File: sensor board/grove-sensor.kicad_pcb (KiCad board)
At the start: 4 copper layers, 50.8 x 50.8 mm, 45 parts, among them P1 CONN_01X01, P2 CONN_01X06, P3 CONN_01X01, P4 CONN_01X01, P5 CONN_01X01, P6 CONN_01X01, P7 CONN_01X01, P8 CONN_01X01, P9 CONN_01X01, Q1 Q_NPN_BEC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

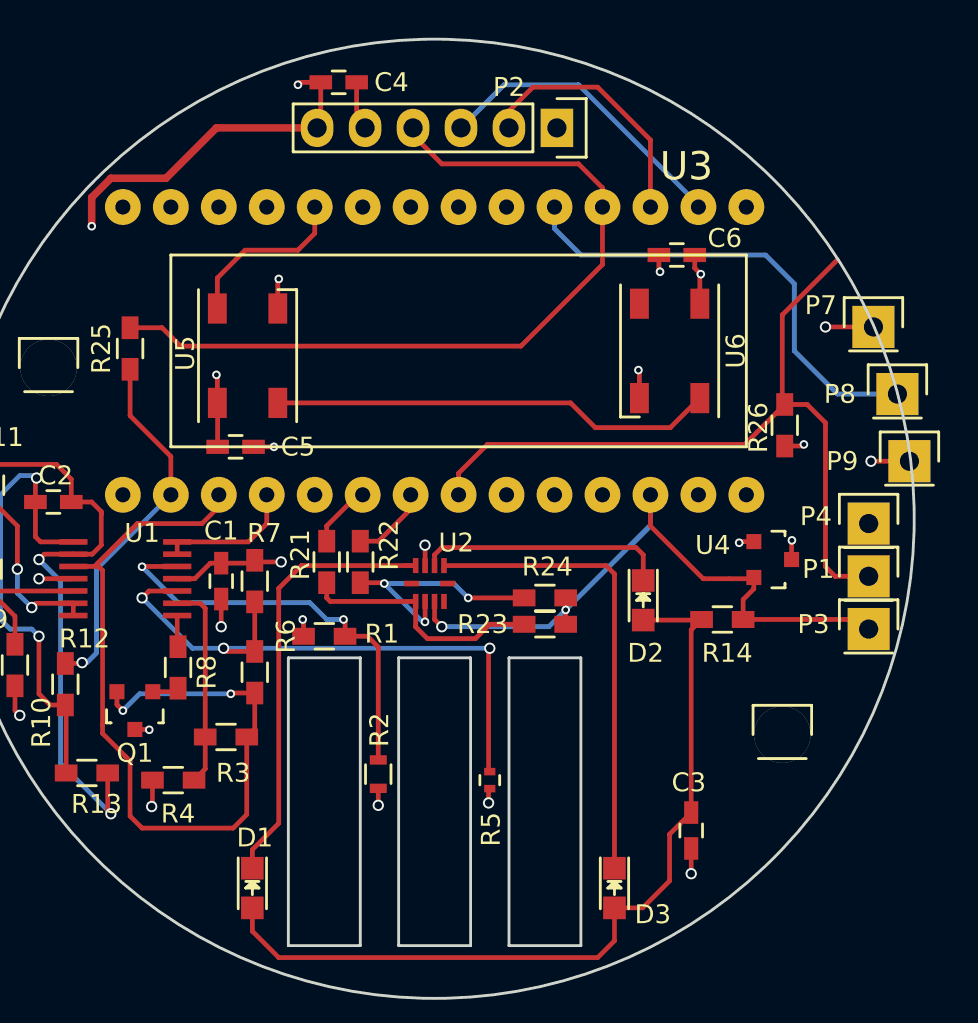
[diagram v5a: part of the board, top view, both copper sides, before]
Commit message: Changes for rev 2 of sensor board
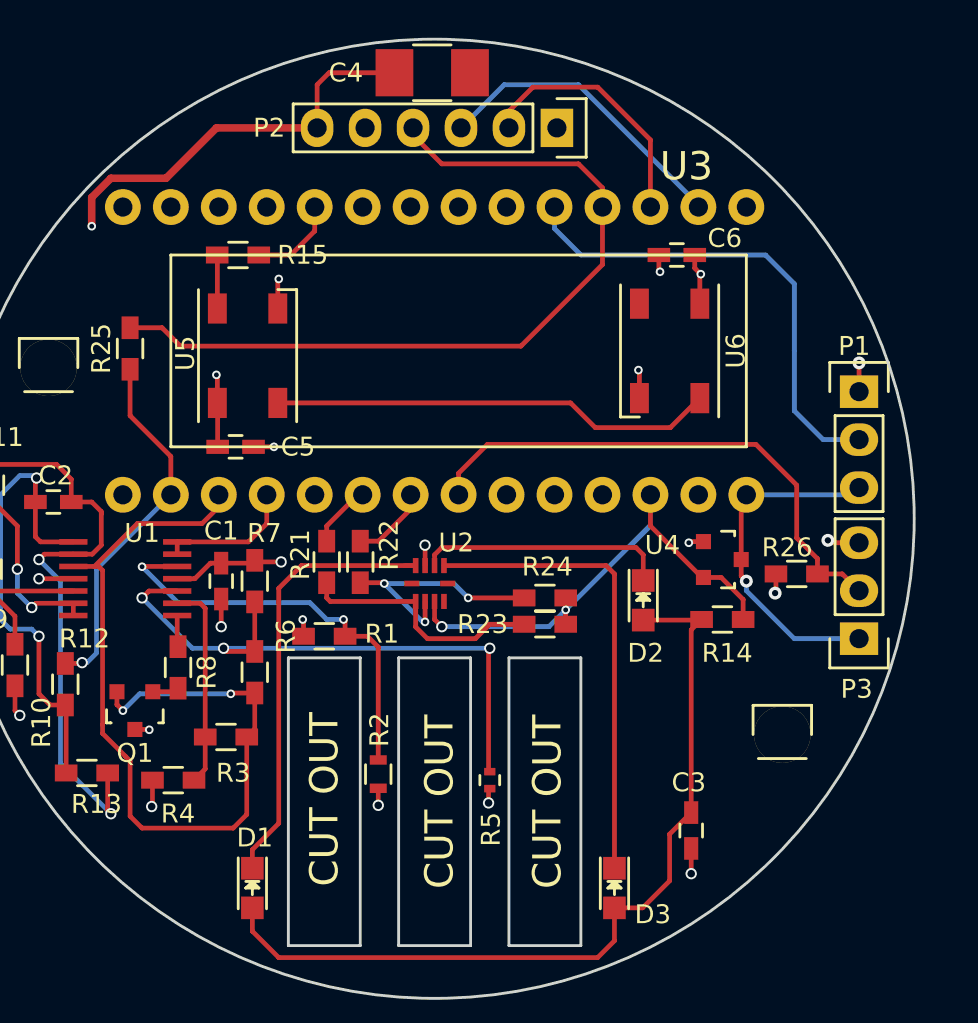
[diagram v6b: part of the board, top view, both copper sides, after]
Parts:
- removed P4, P7, P8, P9: CONN_01X01, Pin_Headers:Pin_Header_Straight_1x01
- added R15: 300, Resistors_SMD:R_0603_HandSoldering, F.Cu at (138.2, 78.7)
- C4: value 10uF -> 100uF; footprint Capacitors_SMD:C_0603_HandSoldering -> Capacitors_SMD:C_1210_HandSoldering
- P1, P3: value CONN_01X01 -> CONN_01X03; footprint Pin_Headers:Pin_Header_Straight_1x01 -> Pin_Headers:Pin_Header_Straight_1x03
- moved P1 9.79 mm to (171.1, 86.0)
- moved R26 7.90 mm to (167.8, 95.6), turned to 0 degrees
- moved C4 4.98 mm to (148.5, 69.1)
- moved U4 2.67 mm to (163.8, 94.9)
- moved P3 0.72 mm to (171.1, 99.1), turned to 180 degrees
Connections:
- P1 pad 1: /PIR_IN -> GND
- P3 pad 1: /3.3V -> +5V
- U3 pad 3: Net-(P8-Pad1) -> Net-(P1-Pad2)
- U3 pad 8: /LED_IN -> Net-(R15-Pad2)
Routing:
- net Net-(P1-Pad2): track 0.00 -> 25.8 mm
- net Net-(P8-Pad1): track 25.0 -> 0.00 mm
- net +5V: track 37.5 -> 55.6 mm, vias 10 -> 8
- net /PIR_IN: track 41.4 -> 28.3 mm
- net /3.3V: track 38.5 -> 30.2 mm
- net /LED_IN: track 9.15 -> 2.84 mm
- net Net-(R15-Pad2): track 0.00 -> 4.76 mm
- net GND: track 22.3 -> 21.3 mm, vias 15 -> 16
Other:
- net class Default: clearance 0.127 -> 0.1524; trace_width 0.4 -> 0.254; via_dia 0.4572 -> 0.6858; via_drill 0.254 -> 0.3302
- net class Power removed
- rule trace_clearance: 0.127 -> 0.1524
- rule trace_min: 0.127 -> 0.1524
- rule via_min_drill: 0.254 -> 0.3302
- rule via_min_size: 0.4572 -> 0.6858
- board text added: "CUT OUT"

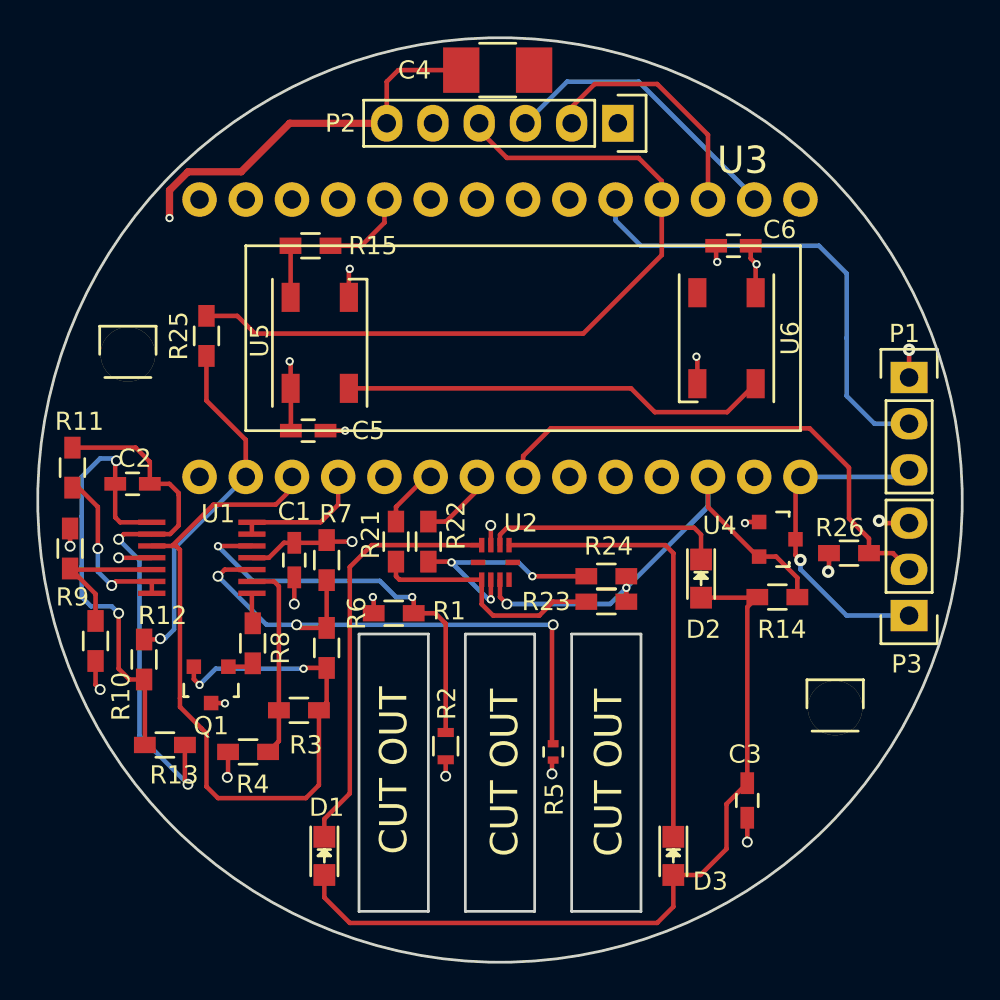
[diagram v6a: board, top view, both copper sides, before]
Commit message: Removed old gerbers, added v2
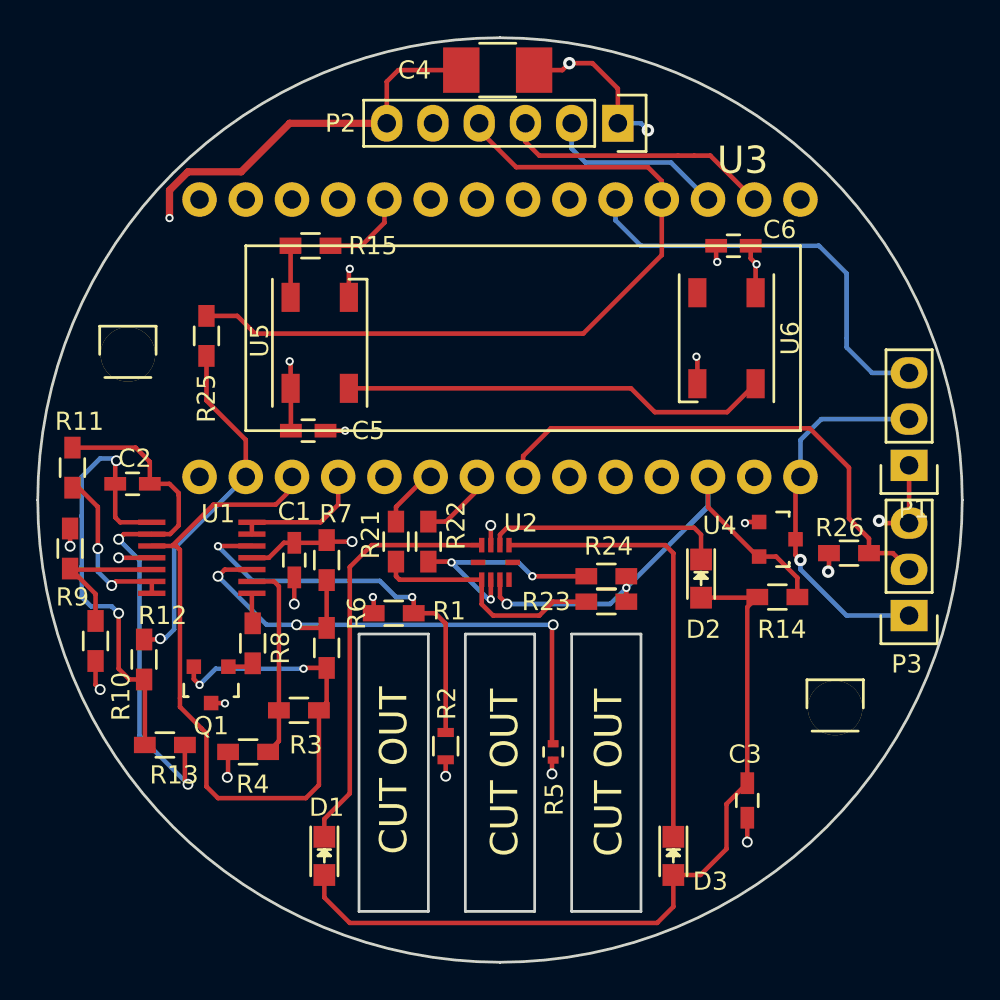
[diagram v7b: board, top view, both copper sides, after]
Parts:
- moved P1 4.83 mm to (171.1, 90.8), turned to 180 degrees
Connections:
- P1 pad 2: Net-(P1-Pad2) -> +5V
- P1 pad 3: +5V -> Net-(P1-Pad3)
- P5 pad 1: Net-(P5-Pad1) -> (no net)
- P6 pad 1: Net-(P6-Pad1) -> (no net)
- U2 pad 10: Net-(U2-Pad10) -> (no net)
- U2 pad 4: Net-(U2-Pad4) -> (no net)
- U2 pad 5: Net-(U2-Pad5) -> (no net)
- U3 pad 10: Net-(U3-Pad10) -> (no net)
- U3 pad 11: Net-(U3-Pad11) -> (no net)
- U3 pad 12: Net-(U3-Pad12) -> (no net)
- U3 pad 13: Net-(U3-Pad13) -> (no net)
- U3 pad 17: Net-(U3-Pad17) -> (no net)
- U3 pad 21: Net-(U3-Pad21) -> (no net)
- U3 pad 22: Net-(U3-Pad22) -> (no net)
- U3 pad 23: Net-(U3-Pad23) -> (no net)
- U3 pad 3: Net-(P1-Pad2) -> Net-(P1-Pad3)
- U3 pad 4: Net-(U3-Pad4) -> (no net)
- U3 pad 5: Net-(U3-Pad5) -> (no net)
- U3 pad 6: Net-(U3-Pad6) -> (no net)
- U3 pad 7: Net-(U3-Pad7) -> (no net)
- U3 pad 9: Net-(U3-Pad9) -> (no net)
- U6 pad 2: Net-(U6-Pad2) -> (no net)
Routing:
- net Net-(P1-Pad2): track 25.8 -> 0.00 mm
- net Net-(P1-Pad3): track 0.00 -> 23.1 mm
- net GND: track 21.3 -> 32.2 mm, vias 16 -> 17
- net Net-(P2-Pad2): track 13.6 -> 10.9 mm
- net +5V: track 55.6 -> 57.9 mm
- net Net-(P2-Pad3): track 16.3 -> 15.0 mm
- net (no net): track 0.00 -> 0.89 mm
- net Net-(U3-Pad11): track 0.76 -> 0.00 mm
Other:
- outline, holes or cut-outs redrawn
- net class Default: clearance 0.1524 -> 0.127; via_dia 0.6858 -> 0.35; via_drill 0.3302 -> 0.25
- rule trace_clearance: 0.1524 -> 0.127
